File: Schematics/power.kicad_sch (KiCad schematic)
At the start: 7 parts, among them IC1 LM3940IS-3.3_NOPB

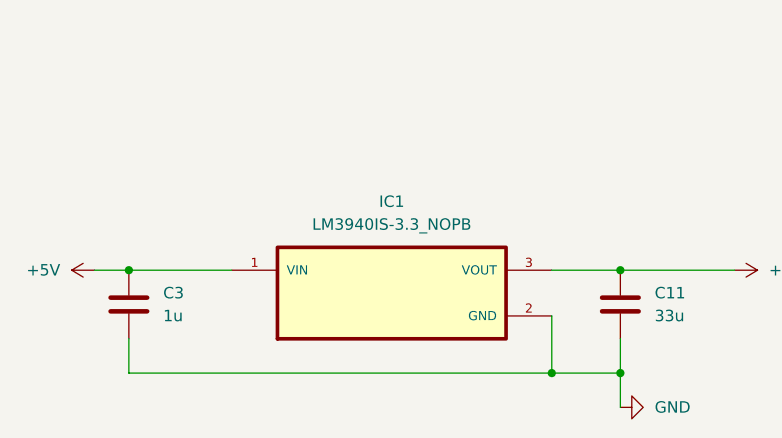
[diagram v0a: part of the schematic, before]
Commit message: Replaced LDO with smaller & Fixed resistor value for Camera tx lines
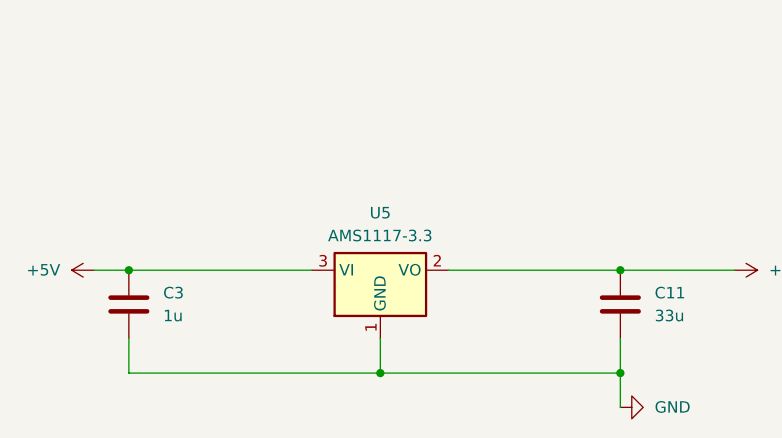
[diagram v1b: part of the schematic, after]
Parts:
- removed IC1: LM3940IS-3.3_NOPB, myFootprints:TO254P1524X483-4N, symbol LM3940IS-3.3_NOPB:LM3940IS-3.3_NOPB
- added U5: AMS1117-3.3, Package_TO_SOT_SMD:SOT-223-3_TabPin2, symbol Regulator_Linear:AMS1117-3.3
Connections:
- net +3.3V: now also U5.2 (VO)
- net +5V: now also U5.3 (VI)
- net GND: now also U5.1 (GND)
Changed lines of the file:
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@@
 	(paper "A4")
-	(junction
-		(at 153.67 106.68)
-		(diameter 0)
-		(color 0 0 0 0)
-	)
 	(junction
 		(at 106.68 95.25)
@@
 		(color 0 0 0 0)
 	)
-	(wire
-		(pts
-			(xy 106.68 106.68) (xy 153.67 106.68)
-		)
-		(stroke
-			(width 0)
-			(type default)
-		)
-	)
-	(wire
-		(pts
-			(xy 153.67 106.68) (xy 161.29 106.68)
+	(junction
+		(at 134.62 106.68)
+		(diameter 0)
+		(color 0 0 0 0)
+	)
+	(wire
+		(pts
+			(xy 106.68 106.68) (xy 134.62 106.68)
+		)
+		(stroke
+			(width 0)
+			(type default)
+		)
+	)
+	(wire
+		(pts
+			(xy 134.62 106.68) (xy 161.29 106.68)
 		)
 		(stroke
@@
 	(wire
 		(pts
-			(xy 153.67 95.25) (xy 161.29 95.25)
+			(xy 134.62 102.87) (xy 134.62 106.68)
 		)
 		(stroke
@@
 	(wire
 		(pts
-			(xy 106.68 95.25) (xy 118.11 95.25)
+			(xy 106.68 95.25) (xy 127 95.25)
 		)
 		(stroke
@@
 	(wire
 		(pts
-			(xy 153.67 100.33) (xy 153.67 106.68)
-		)
-		(stroke
-			(width 0)
-			(type default)
-		)
-	)
-	(wire
-		(pts
 			(xy 110.49 48.26) (xy 115.57 48.26)
 		)
@@
 		(pts
 			(xy 161.29 95.25) (xy 173.99 95.25)
+		)
+		(stroke
+			(width 0)
+			(type default)
+		)
+	)
+	(wire
+		(pts
+			(xy 142.24 95.25) (xy 161.29 95.25)
 		)
 		(stroke
@@
 	)
 	(symbol
-		(lib_id "LM3940IS-3.3_NOPB:LM3940IS-3.3_NOPB")
-		(at 135.89 97.79 0)
+		(lib_id "Regulator_Linear:AMS1117-3.3")
+		(at 134.62 95.25 0)
 		(unit 1)
 		(exclude_from_sim no)
@@
 		(dnp no)
 		(fields_autoplaced yes)
-		(property "Reference" "IC1"
-			(at 135.89 87.63 0)
-			(effects
-				(font
-					(size 1.27 1.27)
-				)
-			)
-		)
-		(property "Value" "LM3940IS-3.3_NOPB"
-			(at 135.89 90.17 0)
-			(effects
-				(font
-					(size 1.27 1.27)
-				)
-			)
-		)
-		(property "Footprint" "myFootprints:TO254P1524X483-4N"
-			(at 135.89 97.79 0)
-			(effects
-				(font
-					(size 1.27 1.27)
-				)
-				(justify left bottom)
-				(hide yes)
-			)
-		)
-		(property "Datasheet" ""
-			(at 135.89 97.79 0)
-			(effects
-				(font
-					(size 1.27 1.27)
-				)
-				(justify left bottom)
-				(hide yes)
-			)
-		)
-		(property "Description" ""
-			(at 135.89 97.79 0)
+		(property "Reference" "U5"
+			(at 134.62 88.9 0)
+			(effects
+				(font
+					(size 1.27 1.27)
+				)
+			)
+		)
+		(property "Value" "AMS1117-3.3"
+			(at 134.62 91.44 0)
+			(effects
+				(font
+					(size 1.27 1.27)
+				)
+			)
+		)
+		(property "Footprint" "Package_TO_SOT_SMD:SOT-223-3_TabPin2"
+			(at 134.62 90.17 0)
+			(effects
+				(font
+					(size 1.27 1.27)
+				)
+				(hide yes)
+			)
+		)
+		(property "Datasheet" "http://www.advanced-monolithic.com/pdf/ds1117.pdf"
+			(at 137.16 101.6 0)
+			(effects
+				(font
+					(size 1.27 1.27)
+				)
+				(hide yes)
+			)
+		)
+		(property "Description" "1A Low Dropout regulator, positive, 3.3V fixed output, SOT-223"
+			(at 134.62 95.25 0)
 			(effects
 				(font
@@
 			(project ""
 				(path "/65068a32-f105-4204-b50e-234054c5a6d0/480e1df8-14aa-40df-bf4b-17bab0b9775f"
-					(reference "IC1")
-					(unit 1)
-				)
+					(reference "U5")
+					(unit 1)
+				)

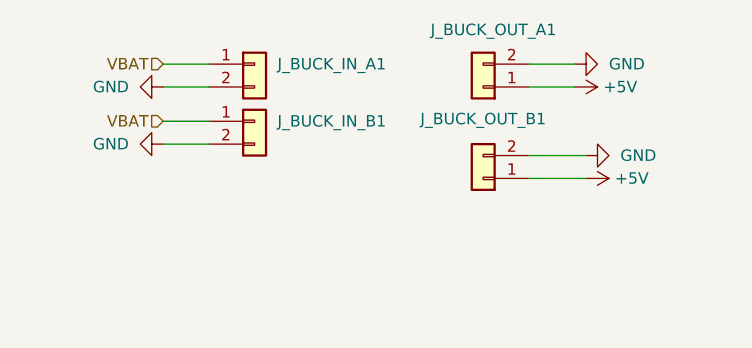
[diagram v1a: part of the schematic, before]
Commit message: Fixed Schematic and PCB refrences everything is connected correctly now
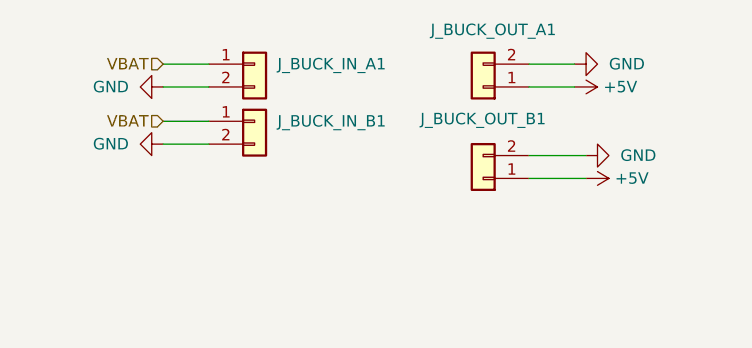
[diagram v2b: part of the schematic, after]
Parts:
- J_BUCK_IN_A1, J_BUCK_IN_B1, J_BUCK_OUT_A1, J_BUCK_OUT_B1: footprint Capacitor_SMD:C_0805_2012Metric_Pad1.18x1.45mm_HandSolder -> Connector_PinSocket_2.54mm:PinSocket_1x02_P2.54mm_Horizontal
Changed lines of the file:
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@@
 			)
 		)
-		(property "Footprint" "Capacitor_SMD:C_0805_2012Metric_Pad1.18x1.45mm_HandSolder"
+		(property "Footprint" "Connector_PinSocket_2.54mm:PinSocket_1x02_P2.54mm_Horizontal"
 			(at 146.05 52.07 0)
 			(effects
@@
 			)
 		)
-		(property "Footprint" "Capacitor_SMD:C_0805_2012Metric_Pad1.18x1.45mm_HandSolder"
+		(property "Footprint" "Connector_PinSocket_2.54mm:PinSocket_1x02_P2.54mm_Horizontal"
 			(at 120.65 45.72 0)
 			(effects
@@
 			)
 		)
-		(property "Footprint" "Capacitor_SMD:C_0805_2012Metric_Pad1.18x1.45mm_HandSolder"
+		(property "Footprint" "Connector_PinSocket_2.54mm:PinSocket_1x02_P2.54mm_Horizontal"
 			(at 146.05 41.91 0)
 			(effects
@@
 		(on_board yes)
 		(dnp no)
-		(fields_autoplaced yes)
 		(property "Reference" "J_BUCK_IN_A1"
-			(at 123.19 39.3699 0)
+			(at 123.19 39.37 0)
 			(effects
 				(font
@@
 			)
 		)
-		(property "Footprint" "Capacitor_SMD:C_0805_2012Metric_Pad1.18x1.45mm_HandSolder"
+		(property "Footprint" "Connector_PinSocket_2.54mm:PinSocket_1x02_P2.54mm_Horizontal"
 			(at 120.65 39.37 0)
 			(effects

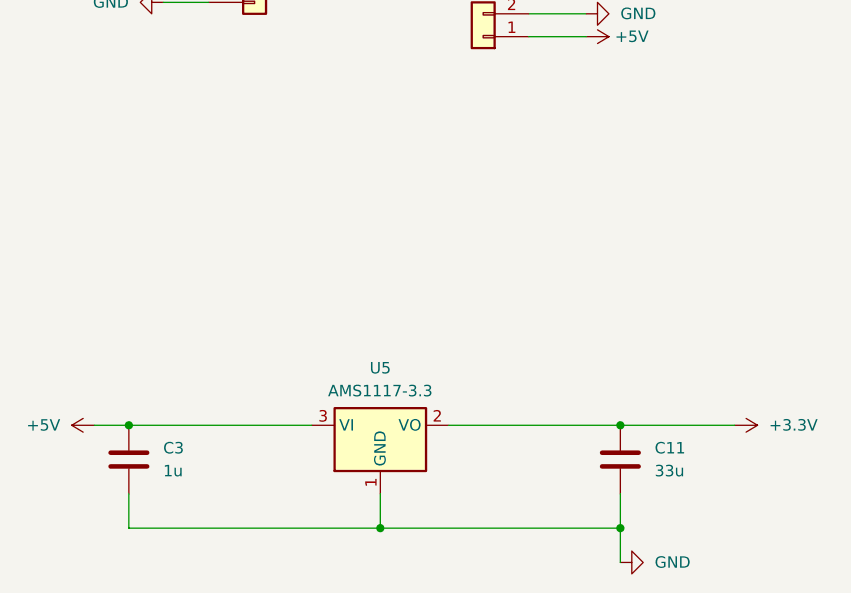
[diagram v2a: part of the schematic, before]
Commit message: fixed all refrences from shematic to pcb and added LED
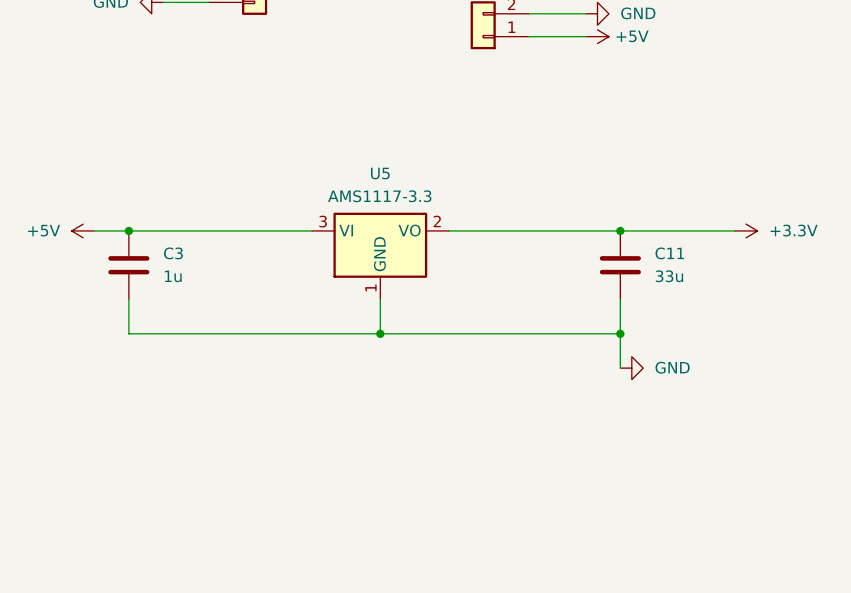
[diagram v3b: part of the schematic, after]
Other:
- moved on the sheet: C11, C3, U5
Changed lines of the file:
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@@
 	(paper "A4")
 	(junction
-		(at 106.68 95.25)
+		(at 106.68 73.66)
 		(diameter 0)
 		(color 0 0 0 0)
 	)
 	(junction
-		(at 161.29 95.25)
+		(at 161.29 73.66)
 		(diameter 0)
 		(color 0 0 0 0)
 	)
 	(junction
-		(at 161.29 106.68)
+		(at 161.29 85.09)
 		(diameter 0)
 		(color 0 0 0 0)
 	)
 	(junction
-		(at 134.62 106.68)
+		(at 134.62 85.09)
 		(diameter 0)
 		(color 0 0 0 0)
@@
 	(wire
 		(pts
-			(xy 106.68 106.68) (xy 134.62 106.68)
-		)
-		(stroke
-			(width 0)
-			(type default)
-		)
-	)
-	(wire
-		(pts
-			(xy 134.62 106.68) (xy 161.29 106.68)
+			(xy 106.68 85.09) (xy 134.62 85.09)
+		)
+		(stroke
+			(width 0)
+			(type default)
+		)
+	)
+	(wire
+		(pts
+			(xy 134.62 85.09) (xy 161.29 85.09)
 		)
 		(stroke
@@
 	(wire
 		(pts
-			(xy 161.29 110.49) (xy 161.29 106.68)
+			(xy 161.29 88.9) (xy 161.29 85.09)
 		)
 		(stroke
@@
 	(wire
 		(pts
-			(xy 134.62 102.87) (xy 134.62 106.68)
-		)
-		(stroke
-			(width 0)
-			(type default)
-		)
-	)
-	(wire
-		(pts
-			(xy 161.29 106.68) (xy 161.29 102.87)
-		)
-		(stroke
-			(width 0)
-			(type default)
-		)
-	)
-	(wire
-		(pts
-			(xy 102.87 95.25) (xy 106.68 95.25)
-		)
-		(stroke
-			(width 0)
-			(type default)
-		)
-	)
-	(wire
-		(pts
-			(xy 106.68 106.68) (xy 106.68 102.87)
+			(xy 134.62 81.28) (xy 134.62 85.09)
+		)
+		(stroke
+			(width 0)
+			(type default)
+		)
+	)
+	(wire
+		(pts
+			(xy 161.29 85.09) (xy 161.29 81.28)
+		)
+		(stroke
+			(width 0)
+			(type default)
+		)
+	)
+	(wire
+		(pts
+			(xy 102.87 73.66) (xy 106.68 73.66)
+		)
+		(stroke
+			(width 0)
+			(type default)
+		)
+	)
+	(wire
+		(pts
+			(xy 106.68 85.09) (xy 106.68 81.28)
 		)
 		(stroke
@@
 	(wire
 		(pts
-			(xy 106.68 95.25) (xy 127 95.25)
+			(xy 106.68 73.66) (xy 127 73.66)
 		)
 		(stroke
@@
 	(wire
 		(pts
-			(xy 161.29 95.25) (xy 173.99 95.25)
-		)
-		(stroke
-			(width 0)
-			(type default)
-		)
-	)
-	(wire
-		(pts
-			(xy 142.24 95.25) (xy 161.29 95.25)
+			(xy 161.29 73.66) (xy 173.99 73.66)
+		)
+		(stroke
+			(width 0)
+			(type default)
+		)
+	)
+	(wire
+		(pts
+			(xy 142.24 73.66) (xy 161.29 73.66)
 		)
 		(stroke
@@
 	(symbol
 		(lib_id "power:+5V")
-		(at 102.87 95.25 90)
+		(at 102.87 73.66 90)
 		(unit 1)
 		(exclude_from_sim no)
@@
 		(fields_autoplaced yes)
 		(property "Reference" "#PWR022"
-			(at 106.68 95.25 0)
+			(at 106.68 73.66 0)
 			(effects
 				(font
@@
 		)
 		(property "Value" "+5V"
-			(at 99.06 95.2499 90)
+			(at 99.06 73.6599 90)
 			(effects
 				(font
@@
 		)
 		(property "Footprint" ""
-			(at 102.87 95.25 0)
+			(at 102.87 73.66 0)
 			(effects
 				(font
@@
 		)
 		(property "Datasheet" ""
-			(at 102.87 95.25 0)
+			(at 102.87 73.66 0)
 			(effects
 				(font
@@
 		)
 		(property "Description" "Power symbol creates a global label with name \"+5V\""
-			(at 102.87 95.25 0)
+			(at 102.87 73.66 0)
 			(effects
 				(font
@@
 	(symbol
 		(lib_id "Device:C")
-		(at 161.29 99.06 0)
+		(at 161.29 77.47 0)
 		(unit 1)
 		(exclude_from_sim no)
@@
 		(dnp no)
 		(property "Reference" "C11"
-			(at 165.1 97.7899 0)
+			(at 165.1 76.1999 0)
 			(effects
 				(font
@@
 		)
 		(property "Value" "33u"
-			(at 165.1 100.3299 0)
+			(at 165.1 78.7399 0)
 			(effects
 				(font
@@
 		)
 		(property "Footprint" "Capacitor_SMD:C_0805_2012Metric_Pad1.18x1.45mm_HandSolder"
-			(at 162.2552 102.87 0)
+			(at 162.2552 81.28 0)
 			(effects
 				(font
@@
 		)
 		(property "Datasheet" "~"
-			(at 161.29 99.06 0)
+			(at 161.29 77.47 0)
 			(effects
 				(font
@@
 		)
 		(property "Description" "Unpolarized capacitor"
-			(at 161.29 99.06 0)
+			(at 161.29 77.47 0)
 			(effects
 				(font
@@
 	(symbol
 		(lib_id "Device:C")
-		(at 106.68 99.06 0)
+		(at 106.68 77.47 0)
 		(unit 1)
 		(exclude_from_sim no)
@@
 		(fields_autoplaced yes)
 		(property "Reference" "C3"
-			(at 110.49 97.7899 0)
+			(at 110.49 76.1999 0)
 			(effects
 				(font
@@
 		)
 		(property "Value" "1u"
-			(at 110.49 100.3299 0)
+			(at 110.49 78.7399 0)
 			(effects
 				(font
@@
 		)
 		(property "Footprint" "Capacitor_SMD:C_0805_2012Metric_Pad1.18x1.45mm_HandSolder"
-			(at 107.6452 102.87 0)
+			(at 107.6452 81.28 0)
 			(effects
 				(font
@@
 		)
 		(property "Datasheet" "~"
-			(at 106.68 99.06 0)
+			(at 106.68 77.47 0)
 			(effects
 				(font
@@
 		)
 		(property "Description" "Unpolarized capacitor"
-			(at 106.68 99.06 0)
+			(at 106.68 77.47 0)
 			(effects
 				(font
@@
 	(symbol
 		(lib_id "Regulator_Linear:AMS1117-3.3")
-		(at 134.62 95.25 0)
+		(at 134.62 73.66 0)
 		(unit 1)
 		(exclude_from_sim no)
@@
 		(fields_autoplaced yes)
 		(property "Reference" "U5"
-			(at 134.62 88.9 0)
+			(at 134.62 67.31 0)
 			(effects
 				(font
@@
 		)
 		(property "Value" "AMS1117-3.3"
-			(at 134.62 91.44 0)
+			(at 134.62 69.85 0)
 			(effects
 				(font
@@
 		)
 		(property "Footprint" "Package_TO_SOT_SMD:SOT-223-3_TabPin2"
-			(at 134.62 90.17 0)
+			(at 134.62 68.58 0)
 			(effects
 				(font
@@
 		)
 		(property "Datasheet" "http://www.advanced-monolithic.com/pdf/ds1117.pdf"
-			(at 137.16 101.6 0)
+			(at 137.16 80.01 0)
 			(effects
 				(font
@@
 		)
 		(property "Description" "1A Low Dropout regulator, positive, 3.3V fixed output, SOT-223"
-			(at 134.62 95.25 0)
+			(at 134.62 73.66 0)
 			(effects
 				(font
@@
 	(symbol
 		(lib_id "power:GND")
-		(at 161.29 110.49 90)
+		(at 161.29 88.9 90)
 		(unit 1)
 		(exclude_from_sim no)
@@
 		(fields_autoplaced yes)
 		(property "Reference" "#PWR09"
-			(at 167.64 110.49 0)
+			(at 167.64 88.9 0)
 			(effects
 				(font
@@
 		)
 		(property "Value" "GND"
-			(at 165.1 110.4899 90)
+			(at 165.1 88.8999 90)
 			(effects
 				(font
@@
 		)
 		(property "Footprint" ""
-			(at 161.29 110.49 0)
+			(at 161.29 88.9 0)
 			(effects
 				(font
@@
 		)
 		(property "Datasheet" ""
-			(at 161.29 110.49 0)
+			(at 161.29 88.9 0)
 			(effects
 				(font
@@
 		)
 		(property "Description" "Power symbol creates a global label with name \"GND\" , ground"
-			(at 161.29 110.49 0)
+			(at 161.29 88.9 0)
 			(effects
 				(font
@@
 	(symbol
 		(lib_id "power:+3.3V")
-		(at 173.99 95.25 270)
+		(at 173.99 73.66 270)
 		(unit 1)
 		(exclude_from_sim no)
@@
 		(fields_autoplaced yes)
 		(property "Reference" "#PWR021"
-			(at 170.18 95.25 0)
+			(at 170.18 73.66 0)
 			(effects
 				(font
@@
 		)
 		(property "Value" "+3.3V"
-			(at 177.8 95.2499 90)
+			(at 177.8 73.6599 90)
 			(effects
 				(font
@@
 		)
 		(property "Footprint" ""
-			(at 173.99 95.25 0)
+			(at 173.99 73.66 0)
 			(effects
 				(font
@@
 		)
 		(property "Datasheet" ""
-			(at 173.99 95.25 0)
+			(at 173.99 73.66 0)
 			(effects
 				(font
@@
 		)
 		(property "Description" "Power symbol creates a global label with name \"+3.3V\""
-			(at 173.99 95.25 0)
-			(effects
-				(font
+			(at 173.99 73.66 0)
+			(effects
+				(font
